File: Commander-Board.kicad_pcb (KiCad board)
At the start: 2 copper layers, 99.1 x 99.1 mm, 9 parts, among them M1 3.5_TFT_SPI_480_320, U1 AMS1117-3.3, U2 ACS711xLCTR-12AB, U3 ESP32-WROOM-32

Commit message: First board test
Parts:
- added C1: 100u, Capacitor_THT:CP_Radial_D10.0mm_P5.00mm, B.Cu at (113.0, 108.0)
- added C3: 1u, Capacitor_THT:C_Disc_D4.7mm_W2.5mm_P5.00mm, B.Cu at (209.6, 109.2)
- added C4: 100n, Capacitor_THT:C_Disc_D4.7mm_W2.5mm_P5.00mm, B.Cu at (41.9, 67.3)
- added C5: 2.2u, Capacitor_THT:C_Disc_D7.0mm_W2.5mm_P5.00mm, B.Cu at (32.8, 79.4)
- added C6: 220u, Capacitor_THT:CP_Radial_D10.0mm_P5.00mm, B.Cu at (118.1, 113.0)
- added C8: C, Capacitor_THT:C_Disc_D4.7mm_W2.5mm_P5.00mm, B.Cu at (41.1, 79.4)
- added C9: 100n, Capacitor_THT:C_Disc_D4.7mm_W2.5mm_P5.00mm, B.Cu at (165.0, 121.9)
- added J1: POWER, TerminalBlock_MetzConnect:TerminalBlock_MetzConnect_Type011_RT05503HBWC_1x03_P5.00mm_Horizontal, B.Cu at (120.6, 85.1)
- added J2: EXPAND, Connector_PinSocket_2.54mm:PinSocket_1x05_P2.54mm_Horizontal, B.Cu at (87.6, 128.3)
- added JP1: BYPASS, Jumper:SolderJumper-2_P1.3mm_Open_RoundedPad1.0x1.5mm, B.Cu at (121.9, 102.9)
- added R1: LDR, OptoDevice:R_LDR_5.1x4.3mm_P3.4mm_Vertical, F.Cu at (124.5, 71.1)
- added R2: 1k, Resistor_THT:R_Axial_DIN0207_L6.3mm_D2.5mm_P10.16mm_Horizontal, B.Cu at (52.7, 58.4)
- added R3: 10k, Resistor_THT:R_Axial_DIN0207_L6.3mm_D2.5mm_P10.16mm_Horizontal, B.Cu at (170.2, 118.1)
- added R4: 10k, Resistor_THT:R_Axial_DIN0207_L6.3mm_D2.5mm_P10.16mm_Horizontal, B.Cu at (146.1, 121.9)
- added R5: 1k, Resistor_THT:R_Axial_DIN0207_L6.3mm_D2.5mm_P10.16mm_Horizontal, B.Cu at (156.2, 118.1)
- added SW1: BUTTON_BACK, Button_Switch_THT:SW_PUSH_6mm_H4.3mm, F.Cu at (81.3, 139.7)
- added SW2: BUTTON_ENTER, Button_Switch_THT:SW_PUSH_6mm_H4.3mm, F.Cu at (168.8, 139.7)
- U1, U2: moved to B.Cu
- moved U3 52.0 mm to (156.2, 104.1), turned to 90 degrees
- moved U1 48.5 mm to (110.5, 95.2), turned to 270 degrees
- moved U2 44.2 mm to (121.9, 95.2), turned to 180 degrees
- moved M1 4.83 mm to (79.1, 131.4)
- moved BOOT 3.18 mm to (132.1, 71.1)
- moved 3V3 3.17 mm to (143.5, 71.1)
- moved GND 3.17 mm to (147.3, 71.1)
- moved RX 3.17 mm to (139.7, 71.1)
- moved TX 3.17 mm to (135.9, 71.1)
- renumbered TP4 to 3V3, TP1 to BOOT, TP5 to GND, TP3 to RX, TP2 to TX
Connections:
- net Net-(U3-Pad29) renamed /SD_CS
- net Net-(U3-Pad30) renamed /SD_SCK
- net Net-(U3-Pad31) renamed /SD_MISO
- net Net-(U3-Pad37) renamed /SD_MOSI
- M1 pad 1: Net-(M1-Pad1) -> (no net)
- M1 pad 10: /TFT_RS -> (no net)
- M1 pad 11: /TFT_RST -> (no net)
- M1 pad 12: /TFT_CS -> (no net)
- M1 pad 13: +3V3 -> (no net)
- M1 pad 14: GND -> (no net)
- M1 pad 15: Net-(M1-Pad15) -> (no net)
- M1 pad 16: Net-(M1-Pad16) -> (no net)
- M1 pad 17: Net-(M1-Pad17) -> (no net)
- M1 pad 18: Net-(M1-Pad18) -> (no net)
- M1 pad 2: Net-(M1-Pad2) -> (no net)
- M1 pad 3: Net-(M1-Pad3) -> (no net)
- M1 pad 4: Net-(M1-Pad4) -> (no net)
- M1 pad 5: Net-(M1-Pad5) -> (no net)
- M1 pad 6: Net-(M1-Pad6) -> (no net)
- M1 pad 7: /TFT_BL -> (no net)
- M1 pad 8: /TFT_SCK -> (no net)
- M1 pad 9: /TFT_DI -> (no net)
- U2 pad 7: Net-(U2-Pad7) -> /AN_CURR
- U3 pad 14: Net-(U3-Pad14) -> /EX_3
- U3 pad 27: Net-(U3-Pad27) -> /PB_ENT
- U3 pad 28: Net-(U3-Pad28) -> /PB_BACK
- U3 pad 33: Net-(U3-Pad33) -> /EX_1
- U3 pad 36: Net-(U3-Pad36) -> /EX_2
- U3 pad 6: Net-(U3-Pad6) -> /AN_VOLT
- U3 pad 8: /PB_ENT -> /AN_LIGHT
- U3 pad 9: /PB_BACK -> /AN_CURR
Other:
- board text added: "Bypass"
- board text added: "Commander 1.0 Designed by Riccardo Persello ©2020 OpenAgri"
- board text added: "Expansion board"
- board text added: "SD Card"
- board text added: "Service"
- board text removed: "Commander 1.0"
- board text removed: "Programming port"

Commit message: Complete
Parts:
- added SW3: Rotary_Encoder, ILI9488_Display:RotaryEncoder_Alps_EC16B04, F.Cu at (144.5, 129.5)
- moved C8 136.3 mm to (173.4, 112.5), turned to 270 degrees
- moved R2 114.5 mm to (156.2, 107.3), turned to 270 degrees
- moved C5 105.5 mm to (134.7, 106.7)
- moved C4 94.5 mm to (132.7, 93.4), turned to 270 degrees
- moved C3 74.6 mm to (135.3, 102.2), turned to 180 degrees
- moved SW1 29.2 mm to (110.3, 137.2)
- moved C9 18.8 mm to (181.3, 112.4)
- moved JP1 17.8 mm to (139.7, 101.6), turned to 270 degrees
- moved M1 17.5 mm to (95.9, 126.4)
- moved TP2 17.3 mm to (152.4, 66.0)
- moved TP3 17.3 mm to (156.2, 66.0)
- moved TP4 17.3 mm to (160.0, 66.0)
- moved TP5 17.3 mm to (163.8, 66.0)
- moved J2 17.3 mm to (104.1, 123.2)
- moved R1 17.3 mm to (141.0, 66.0)
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- renumbered BOOT to TP1, TX to TP2, RX to TP3, 3V3 to TP4, GND to TP5
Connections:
- M1 pad 1: (no net) -> Net-(M1-Pad1)
- M1 pad 10: (no net) -> /TFT_RS
- M1 pad 11: (no net) -> /TFT_RST
- M1 pad 12: (no net) -> /TFT_CS
- M1 pad 13: (no net) -> +3V3
- M1 pad 14: (no net) -> GND
- M1 pad 15: (no net) -> /SD_CS
- M1 pad 16: (no net) -> /SD_MOSI
- M1 pad 17: (no net) -> /SD_MISO
- M1 pad 18: (no net) -> /SD_SCK
- M1 pad 2: (no net) -> Net-(M1-Pad2)
- M1 pad 3: (no net) -> Net-(M1-Pad3)
- M1 pad 4: (no net) -> Net-(M1-Pad4)
- M1 pad 5: (no net) -> Net-(M1-Pad5)
- M1 pad 6: (no net) -> Net-(M1-Pad6)
- M1 pad 7: (no net) -> /TFT_BL
- M1 pad 8: (no net) -> /TFT_SCK
- M1 pad 9: (no net) -> /TFT_DI
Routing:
- net /PB_BACK: track 0.00 -> 104.2 mm, vias 0 -> 1
- net /EX_2: track 0.00 -> 103.7 mm, vias 0 -> 2
- net /EX_1: track 0.00 -> 102.8 mm, vias 0 -> 2
- net /TFT_BL: track 0.00 -> 77.5 mm, vias 0 -> 1
- net /TFT_SCK: track 0.00 -> 74.6 mm, vias 0 -> 1
- net /TFT_RST: track 0.00 -> 70.9 mm, vias 0 -> 1
- net /TFT_CS: track 0.00 -> 70.0 mm, vias 0 -> 1
- net /EX_3: track 0.00 -> 69.8 mm
- net /TFT_DI: track 0.00 -> 69.8 mm, vias 0 -> 1
- net /TFT_RS: track 0.00 -> 68.2 mm, vias 0 -> 1
- net /AN_LIGHT: track 0.00 -> 67.5 mm, vias 0 -> 1
- net /PB_ENT: track 0.00 -> 56.9 mm, vias 0 -> 1
- net /AN_CURR: track 0.00 -> 52.5 mm, vias 0 -> 2
- net Net-(J1-Pad2): track 0.00 -> 50.8 mm
- net /ENC_B: track 0.00 -> 41.2 mm
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- added copper zone on B.Cu, net +12V
- added copper zone on B.Cu, net +3V3
- added copper zone on F.Cu, net GND
- added copper zone on B.Cu, net Net-(J1-Pad1)
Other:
- board size 99.1 x 99.1 mm -> 98.4 x 98.4 mm
- board text added: "Power supply"

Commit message: Minor fixes
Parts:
- added  : MountingHole_3.2mm_M3, MountingHole:MountingHole_3.2mm_M3, F.Cu at (109.2, 76.2)
- added  : MountingHole_3.2mm_M3, MountingHole:MountingHole_3.2mm_M3, F.Cu at (188.6, 144.1)
- added  : MountingHole_3.2mm_M3, MountingHole:MountingHole_3.2mm_M3, F.Cu at (100.3, 144.1)
- added  : MountingHole_3.2mm_M3, MountingHole:MountingHole_3.2mm_M3, F.Cu at (188.6, 55.9)
- added  : MountingHole_3.2mm_M3, MountingHole:MountingHole_3.2mm_M3, F.Cu at (100.3, 55.9)

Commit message: Minor corrections
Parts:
- added  : , ILI9488_Display:QRCODE, B.Cu at (126.4, 135.3)
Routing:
- net /PB_BACK: track 104.2 -> 105.1 mm
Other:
- board text added: "Commander 1.0 Riccardo Persello ©2020 OpenAgri Model number TKC1 Board S/N: JLCJLCJLCJLC"
- board text removed: "Commander 1.0 Designed by Riccardo Persello ©2020 OpenAgri"

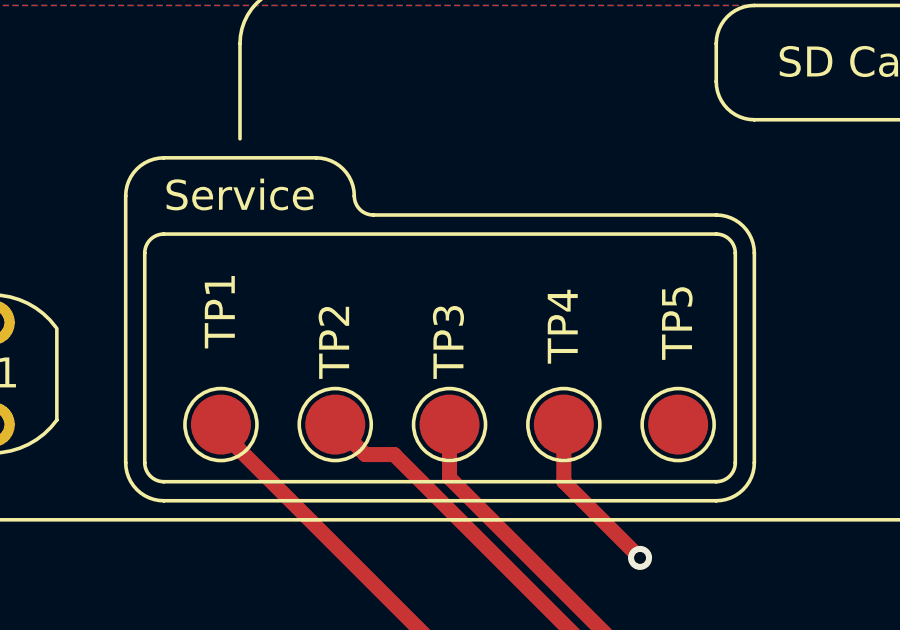
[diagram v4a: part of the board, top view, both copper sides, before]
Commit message: Added service labels
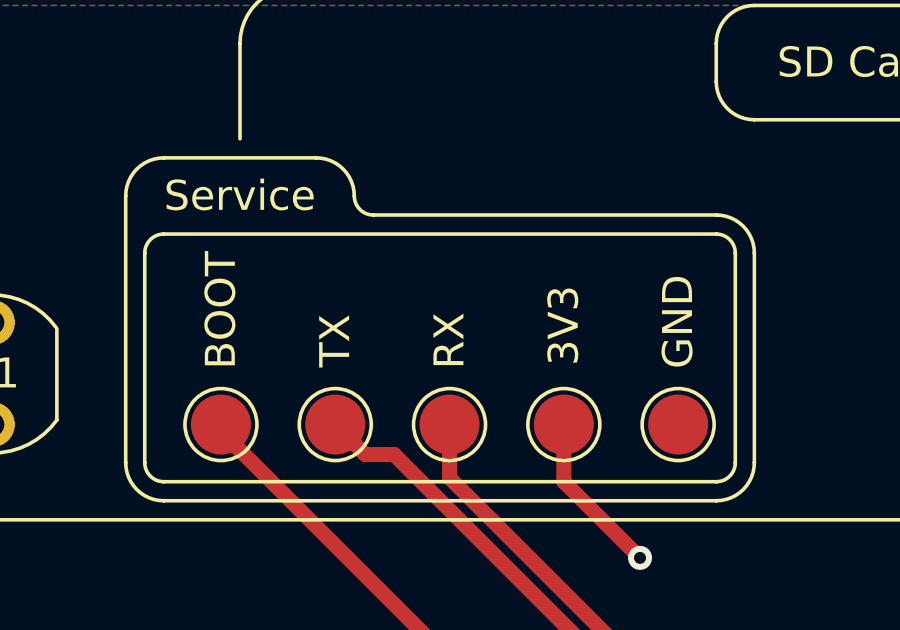
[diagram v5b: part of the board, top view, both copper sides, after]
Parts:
- renumbered TP4 to 3V3, TP1 to BOOT, TP5 to GND, TP3 to RX, TP2 to TX
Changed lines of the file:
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@@
-(kicad_pcb (version 20171130) (host pcbnew 5.1.5+dfsg1-2build2)
+(kicad_pcb (version 20171130) (host pcbnew "(5.1.5-0-10_14)")
   (general
     (thickness 1.6)
@@
   )
   (setup
-    (last_trace_width 0.5)
+    (last_trace_width 0.25)
     (user_trace_width 0.25)
     (user_trace_width 0.33)
@@
     (tags "test point SMD pad")
     (attr virtual)
-    (fp_text reference TP1 (at 0 -3.81 90) (layer F.SilkS)
+    (fp_text reference BOOT (at 0 -3.81 90) (layer F.SilkS)
       (effects (font (size 1 1) (thickness 0.15)))
     )
@@
     (tags "test point SMD pad")
     (attr virtual)
-    (fp_text reference TP2 (at 0 -2.794 90) (layer F.SilkS)
+    (fp_text reference TX (at 0 -2.794 90) (layer F.SilkS)
       (effects (font (size 1 1) (thickness 0.15)))
     )
@@
     (tags "test point SMD pad")
     (attr virtual)
-    (fp_text reference TP3 (at 0 -2.794 270) (layer F.SilkS)
+    (fp_text reference RX (at 0 -2.794 90) (layer F.SilkS)
       (effects (font (size 1 1) (thickness 0.15)))
     )
@@
     (tags "test point SMD pad")
     (attr virtual)
-    (fp_text reference TP4 (at 0 -3.302 90) (layer F.SilkS)
+    (fp_text reference 3V3 (at 0 -3.302 90) (layer F.SilkS)
       (effects (font (size 1 1) (thickness 0.15)))
     )
@@
     (tags "test point SMD pad")
     (attr virtual)
-    (fp_text reference TP5 (at 0 -3.429 90) (layer F.SilkS)
-      (effects (font (size 1 1) (thickness 0.15)))
-    )
+    (fp_text reference GND (at 0 -3.429 90) (layer F.SilkS)
+      (effects (font (size 1 1) (thickness 0.15)))
+    )

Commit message: New holes, removed board S/N.
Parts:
- removed the   at (188.6, 144.1)
- removed the   at (100.3, 144.1)
- removed the   at (188.6, 55.9)
- removed the   at (100.3, 55.9)
- added  : MountingHole_3.2mm_M3_DIN965_Pad, MountingHole:MountingHole_3.2mm_M3_DIN965_Pad, F.Cu at (99.7, 144.8)
- added  : MountingHole_3.2mm_M3_DIN965_Pad, MountingHole:MountingHole_3.2mm_M3_DIN965_Pad, F.Cu at (189.2, 144.8)
- added  : MountingHole_3.2mm_M3_DIN965_Pad, MountingHole:MountingHole_3.2mm_M3_DIN965_Pad, F.Cu at (189.2, 55.2)
- added  : MountingHole_3.2mm_M3_DIN965_Pad, MountingHole:MountingHole_3.2mm_M3_DIN965_Pad, F.Cu at (99.7, 55.2)
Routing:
- net (no net): vias 0 -> 32
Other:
- board text added: "Commander 1.0 Riccardo Persello ©2020 OpenAgri Model number TKC1"
- board text removed: "Commander 1.0 Riccardo Persello ©2020 OpenAgri Model number TKC1 Board S/N: JLCJLCJLCJLC"

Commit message: New service connector
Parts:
- removed 3V3: SERVICE_3V3, TestPoint:TestPoint_Pad_D2.0mm
- removed BOOT: SERVICE_BOOT, TestPoint:TestPoint_Pad_D2.0mm
- removed GND: SERVICE_GND, TestPoint:TestPoint_Pad_D2.0mm
- removed the RX at (156.2, 66.0)
- removed the TX at (152.4, 66.0)
- added +: SERVICE_3V3, TestPoint:TestPoint_Pad_D1.0mm, F.Cu at (161.5, 66.3)
- added -: SERVICE_GND, TestPoint:TestPoint_Pad_D1.0mm, F.Cu at (164.1, 66.3)
- added B: SERVICE_BOOT, TestPoint:TestPoint_Pad_D1.0mm, F.Cu at (153.9, 66.3)
- added RX: SERVICE_RX, TestPoint:TestPoint_Pad_D1.0mm, F.Cu at (159.0, 66.3)
- added TX: SERVICE_TX, TestPoint:TestPoint_Pad_D1.0mm, F.Cu at (156.5, 66.3)
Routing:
- net /PR_TX: track 36.5 -> 34.1 mm
- net /PR_BOOT: track 31.5 -> 29.1 mm
- net /PR_RX: track 33.2 -> 31.9 mm

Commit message: Ready for panelization.
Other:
- board text added: "Commander Riccardo Persello ©2020 OpenAgri Model number TKC"
- board text removed: "Commander 1.0 Riccardo Persello ©2020 OpenAgri Model number TKC1"
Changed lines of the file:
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@@
   )
   (setup
-    (last_trace_width 0.5)
+    (last_trace_width 0.25)
     (user_trace_width 0.25)
     (user_trace_width 0.33)
@@
   (gr_line (start 148.59 125.73) (end 148.59 130.81) (layer B.SilkS) (width 0.12))
   (gr_line (start 143.51 125.73) (end 148.59 125.73) (layer B.SilkS) (width 0.12))
-  (gr_text "Commander 1.0\nRiccardo Persello\n©2020 OpenAgri\nModel number TKC1" (at 187.325 130.175) (layer B.SilkS)
+  (gr_text "Commander\nRiccardo Persello\n©2020 OpenAgri\nModel number TKC" (at 187.325 130.175) (layer B.SilkS)
     (effects (font (size 1 1) (thickness 0.15)) (justify left mirror))
   )
